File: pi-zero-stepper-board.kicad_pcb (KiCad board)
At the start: 2 copper layers, 83.8 x 74.3 mm, 20 parts, among them CON1 DC12v, M3_1 MountingHole_3.2mm_M3, M3_2 MountingHole_3.2mm_M3, P1 Servo (A0), P2 Endstop1 (A1), P3 Endstop2 (A2), P4 Stepper1, P5 Stepper2, P6 COM, P7 Aux (D10 - 13)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

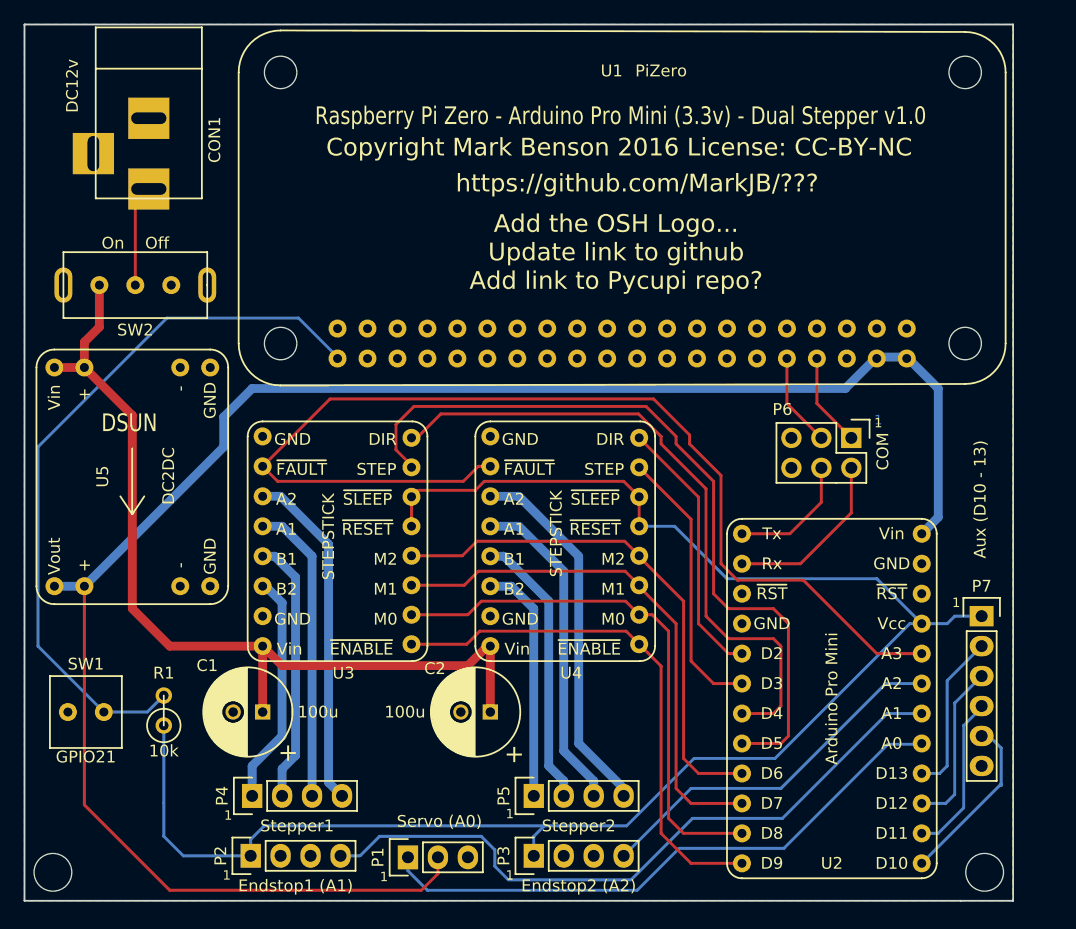
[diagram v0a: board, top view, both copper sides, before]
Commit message: Fixed power track, added I2C and updated brd text
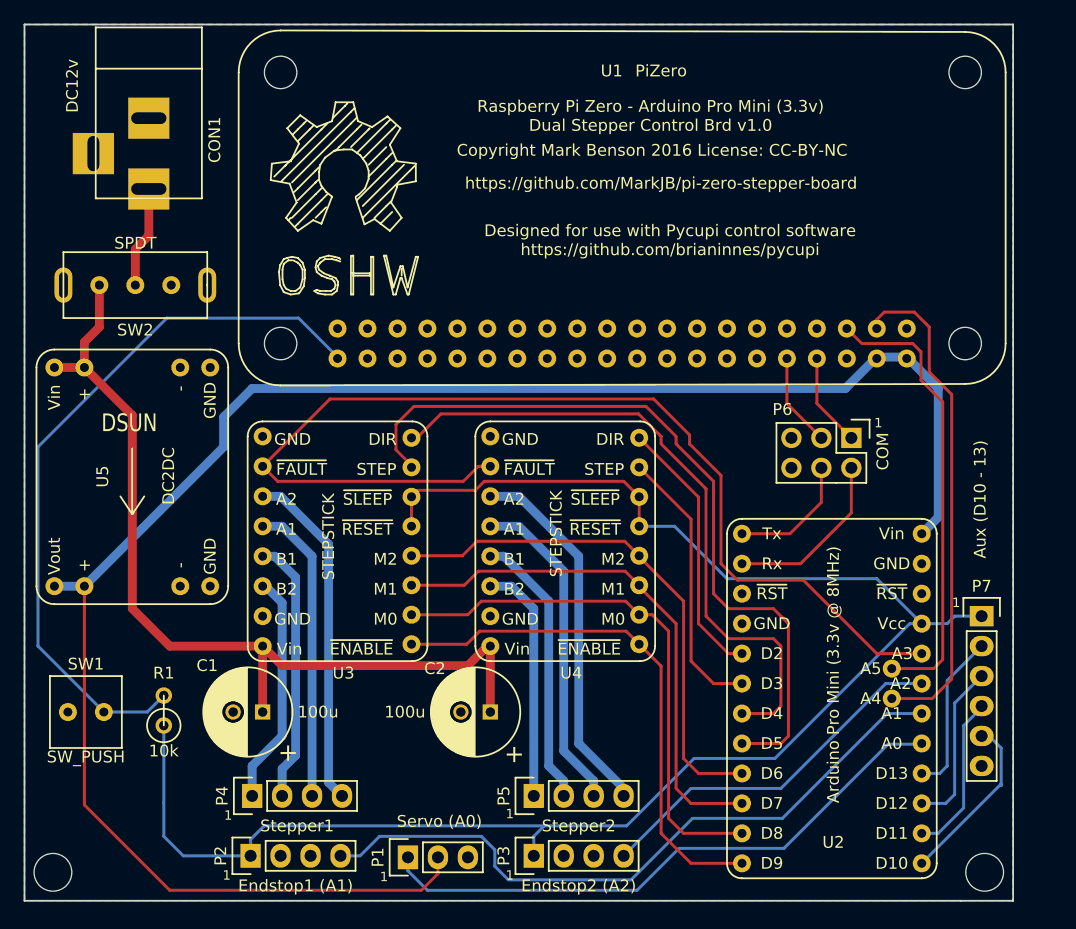
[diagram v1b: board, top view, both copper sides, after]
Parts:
- added REF**: Symbol_OSHW-Logo_SilkScreen_BIG, Symbols:Symbol_OSHW-Logo_SilkScreen_BIG, B.Cu at (119.8, 57.4)
- added REF**: Symbol_OSHW-Logo_SilkScreen_BIG, Symbols:Symbol_OSHW-Logo_SilkScreen_BIG, F.Cu at (120.5, 57.5)
- SW1: value GPIO21 -> SW_PUSH
- SW2: value On Off -> SPDT
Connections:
- U1 pad 3: Net-(U1-Pad3) -> /SDA
- U1 pad 5: Net-(U1-Pad5) -> /SCL
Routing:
- net /SDA: track 0.00 -> 42.4 mm
- net /SCL: track 0.00 -> 38.6 mm
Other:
- board text added: "Designed for use with Pycupi control software https://github.com/brianinnes/pycupi"
- board text added: "Raspberry Pi Zero - Arduino Pro Mini (3.3v) Dual Stepper Control Brd v1.0"
- board text added: "https://github.com/MarkJB/pi-zero-stepper-board"
- board text removed: "Add the OSH Logo... Update link to github Add link to Pycupi repo?"
- board text removed: "Raspberry Pi Zero - Arduino Pro Mini (3.3v) - Dual Stepper v1.0"
- board text removed: "https://github.com/MarkJB/???"

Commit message: Added I2C and other fixes
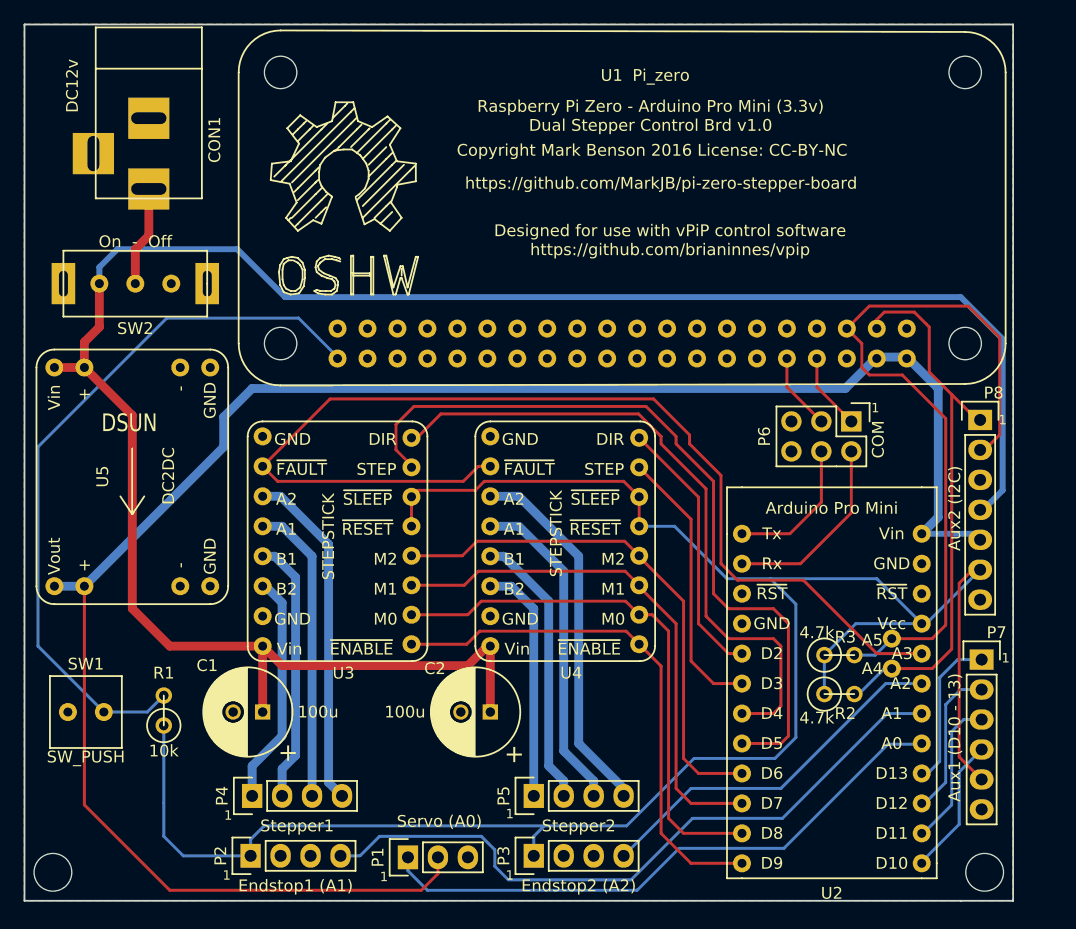
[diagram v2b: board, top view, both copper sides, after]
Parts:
- added P8: Aux2 (I2C), Pin_Headers:Pin_Header_Straight_1x07, F.Cu at (174.4, 97.7)
- added R2: 4.7k, Discret:R1, F.Cu at (162.4, 120.9)
- added R3: 4.7k, Discret:R1, F.Cu at (162.4, 117.6)
- P7: value Aux (D10 - 13) -> Aux1 (D10 - 13)
- SW2: value SPDT -> On - Off
- U1: value PiZero -> Pi_zero
- moved P7 3.68 mm to (174.5, 118.0)
- moved P6 1.40 mm to (163.4, 97.8)
- moved REF** 1.27 mm to (118.5, 57.4)
- moved SW2 0.13 mm to (102.7, 86.1)
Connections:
- P7 pad 1: /3v3 -> /D10
- P7 pad 2: /D10 -> /D11
- P7 pad 3: /D11 -> /D12
- P7 pad 4: /D12 -> /D13
- P7 pad 5: /D13 -> /3v3
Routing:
- net +12V: track 76.4 -> 173.6 mm
- net /3v3: track 145.0 -> 178.5 mm
- net /SCL: track 38.6 -> 64.3 mm
- net /VCC: track 152.0 -> 157.1 mm
- net /SDA: track 42.4 -> 47.2 mm
- net /D13: track 14.9 -> 11.8 mm
- net /ArdTx: track 10.8 -> 12.2 mm
- net /ArdRx: track 14.9 -> 16.3 mm
- net /PiRx: track 7.94 -> 6.54 mm
- net /PiTx: track 7.94 -> 6.54 mm
- net /D10: track 14.4 -> 13.2 mm
- net /D11: track 14.1 -> 12.9 mm
- net /D12: track 13.7 -> 12.7 mm
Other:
- board text added: "12v"
- board text added: "2"
- board text added: "3"
- board text added: "3.3v"
- board text added: "4"
- board text added: "5"
- board text added: "5v"
- board text added: "6"
- board text added: "7"
- board text added: "D10"
- board text added: "D11"
- board text added: "D12"
- board text added: "D13"
- board text added: "Designed for use with vPiP control software https://github.com/brianinnes/vpip"
- board text added: "Func"
- board text added: "GND"
- board text added: "NC"
- board text added: "P7 Aux1 (D10-13)"
- board text added: "P8 Aux2 (I2C)"
- board text added: "Pin"
- board text added: "SCL"
- board text added: "SDA"
- board text removed: "Designed for use with Pycupi control software https://github.com/brianinnes/pycupi"
